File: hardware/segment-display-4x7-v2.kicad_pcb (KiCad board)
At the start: 2 copper layers, 65 x 25 mm, 32 parts, among them P1 CON-SENSOR2, P2 DEBUG, P3 BOOT, U1 XMC1XXX24, U2 TM1637, U3 SEGMENT_4X7, U4 DRILL, U5 DRILL, U6 DRILL, U7 DRILL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

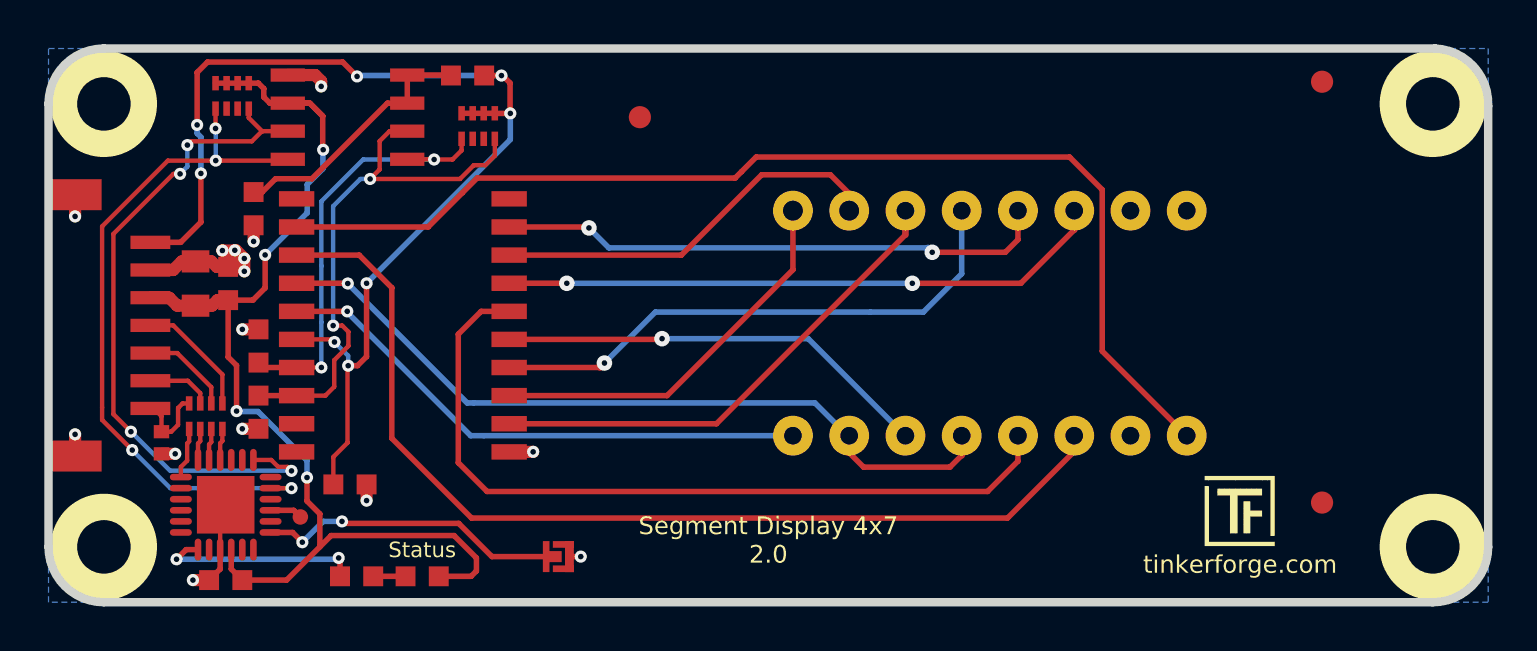
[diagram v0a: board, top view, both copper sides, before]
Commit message: segment driver reconnect, control all available leds
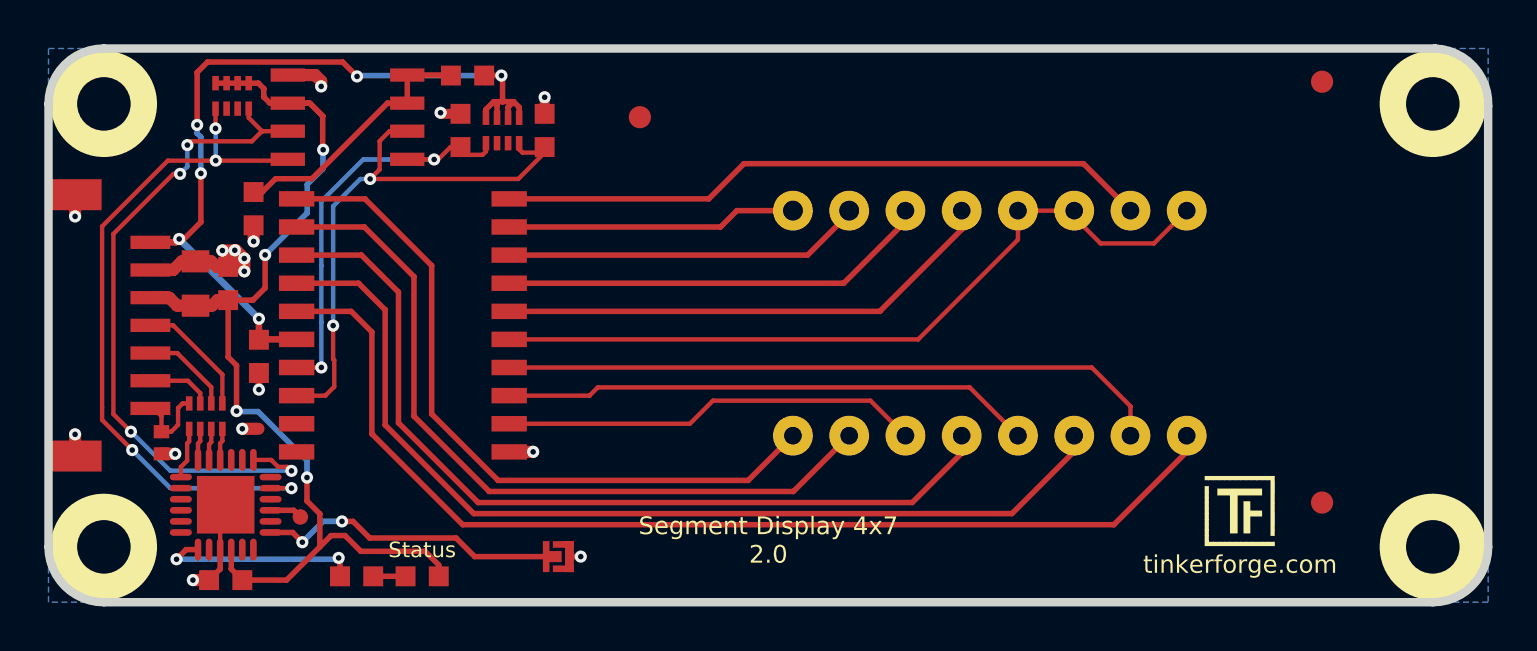
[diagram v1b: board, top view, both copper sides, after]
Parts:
- moved C3 18.1 mm to (65.3, 33.5), turned to 270 degrees
- moved C1 13.3 mm to (61.5, 33.5)
- moved C5 7.09 mm to (52.4, 43.7), turned to 270 degrees
- moved RP2 1.12 mm to (63.4, 33.5)
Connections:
- RP2 pad 6: Net-(RP2-Pad6) -> (no net)
- RP2 pad 7: Net-(RP2-Pad7) -> (no net)
- RP3 pad 6: Net-(RP3-Pad6) -> (no net)
- RP3 pad 7: Net-(RP3-Pad7) -> (no net)
- U1 pad 11: Net-(U1-Pad11) -> (no net)
- U1 pad 12: Net-(U1-Pad12) -> (no net)
- U1 pad 14: Net-(U1-Pad14) -> (no net)
- U1 pad 16: Net-(U1-Pad16) -> (no net)
- U1 pad 18: Net-(U1-Pad18) -> (no net)
- U1 pad 2: Net-(U1-Pad2) -> (no net)
- U1 pad 20: Net-(U1-Pad20) -> (no net)
- U1 pad 21: Net-(U1-Pad21) -> (no net)
- U1 pad 3: Net-(U1-Pad3) -> (no net)
- U1 pad 4: Net-(U1-Pad4) -> (no net)
- U1 pad 5: Net-(U1-Pad5) -> (no net)
- U1 pad 6: Net-(U1-Pad6) -> (no net)
- U1 pad 8: Net-(U1-Pad8) -> (no net)
- U2 pad 10: Net-(U2-Pad10) -> COMD3
- U2 pad 11: Net-(U2-Pad11) -> COM1
- U2 pad 12: COM4 -> COM2
- U2 pad 13: COM3 -> COMD1D2
- U2 pad 14: COM2 -> COM3
- U2 pad 15: COM1 -> COM4
- U2 pad 19: Net-(U2-Pad19) -> (no net)
- U2 pad 20: Net-(U2-Pad20) -> (no net)
- U3 pad 10: Net-(U3-Pad10) -> COMD3
- U3 pad 11: Net-(U2-Pad7) -> Net-(U2-Pad5)
- U3 pad 12: Net-(U2-Pad9) -> Net-(U2-Pad5)
- U3 pad 13: Net-(U2-Pad4) -> Net-(U2-Pad6)
- U3 pad 14: Net-(U2-Pad2) -> Net-(U2-Pad7)
- U3 pad 16: Net-(U2-Pad3) -> Net-(U2-Pad9)
- U3 pad 3: Net-(U2-Pad5) -> Net-(U2-Pad2)
- U3 pad 4: COM2 -> COMD1D2
- U3 pad 5: Net-(U2-Pad6) -> Net-(U2-Pad3)
- U3 pad 7: Net-(U3-Pad7) -> Net-(U2-Pad4)
- U3 pad 9: Net-(U3-Pad9) -> Net-(U2-Pad5)
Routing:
- net COMD1D2: track 0.00 -> 39.8 mm
- net COMD3: track 0.00 -> 29.6 mm
- net Net-(U2-Pad5): track 19.7 -> 35.2 mm, vias 1 -> 0
- net Net-(U2-Pad6): track 36.1 -> 22.8 mm
- net +5V: track 52.1 -> 39.1 mm, vias 8 -> 6
- net Net-(U2-Pad9): track 25.0 -> 13.1 mm, vias 2 -> 0
- net Net-(U2-Pad7): track 27.4 -> 19.5 mm, vias 2 -> 0
- net COM1: track 24.8 -> 32.4 mm, vias 1 -> 0
- net Net-(U2-Pad3): track 17.8 -> 24.0 mm
- net Net-(U2-Pad4): track 25.0 -> 30.1 mm, vias 1 -> 0
- net Net-(U2-Pad2): track 22.5 -> 19.0 mm
- net VCC: track 51.2 -> 47.8 mm
- net COM4: track 51.0 -> 49.0 mm
- net Net-(U2-Pad8): track 18.0 -> 16.3 mm
- net COM3: track 46.0 -> 44.3 mm
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
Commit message: remove open gnd circuit
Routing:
- net GND: track 29.4 -> 28.6 mm, vias 16 -> 15
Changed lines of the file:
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@@
     (thickness 1.6002)
     (drawings 12)
-    (tracks 377)
+    (tracks 375)
     (zones 0)
     (modules 32)
@@
   )
   (setup
-    (last_trace_width 0.25)
+    (last_trace_width 0.2)
     (user_trace_width 0.2)
     (user_trace_width 0.25)
@@
   (segment (start 51.55 51.05) (end 51.55 49.75) (width 0.25) (layer Vorderseite) (net 6))
   (segment (start 51.55 49.75) (end 50.25 49.75) (width 0.25) (layer Vorderseite) (net 6))
-  (segment (start 52.38 46.97) (end 51.65 46.97) (width 0.55) (layer Vorderseite) (net 6))
-  (via (at 51.65 46.97) (size 0.55) (drill 0.25) (layers Vorderseite Rückseite) (net 6))
   (segment (start 63.69806 48.01246) (end 64.77754 48.01246) (width 0.55) (layer Vorderseite) (net 6))
   (segment (start 64.77754 48.01246) (end 64.78 48.01) (width 0.55) (layer Vorderseite) (net 6))
